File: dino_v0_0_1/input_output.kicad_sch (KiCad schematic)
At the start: 25 parts, among them SW1 SW_DIP_x07

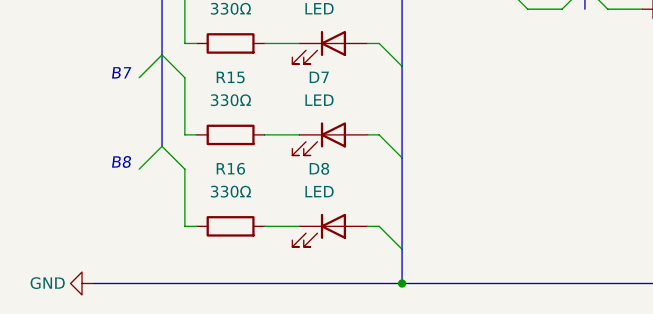
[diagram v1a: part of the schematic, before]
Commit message: Updates schematic with corrections
- Corrects ~CE on 74LS645
- Fixes MCM60256AP DQ6 Pin Number
- Removes "Net Label" for +5V and adds correct text label
- Attaches both GND and VCC to bus proper
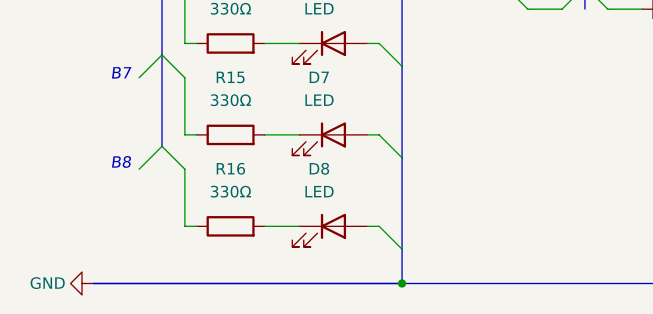
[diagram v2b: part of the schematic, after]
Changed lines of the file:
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@@
 	(title_block
 		(title "Dino v0.0.1")
-		(date "2025-06-15")
-		(rev "v1.0.1")
+		(date "2025-06-30")
+		(rev "v1.0.2")
 		(comment 1 "Input Output Components")
 		(comment 3 "Utilizes a 555 timer and binary counter to increment addressing.")
@@
 		)
 		(stroke
+			(width 0)
+			(type default)
+			(color 0 0 0 1)
+		)
+	)
+	(bus
+		(pts
+			(xy 24.13 119.38) (xy 58.42 119.38)
+		)
+		(stroke

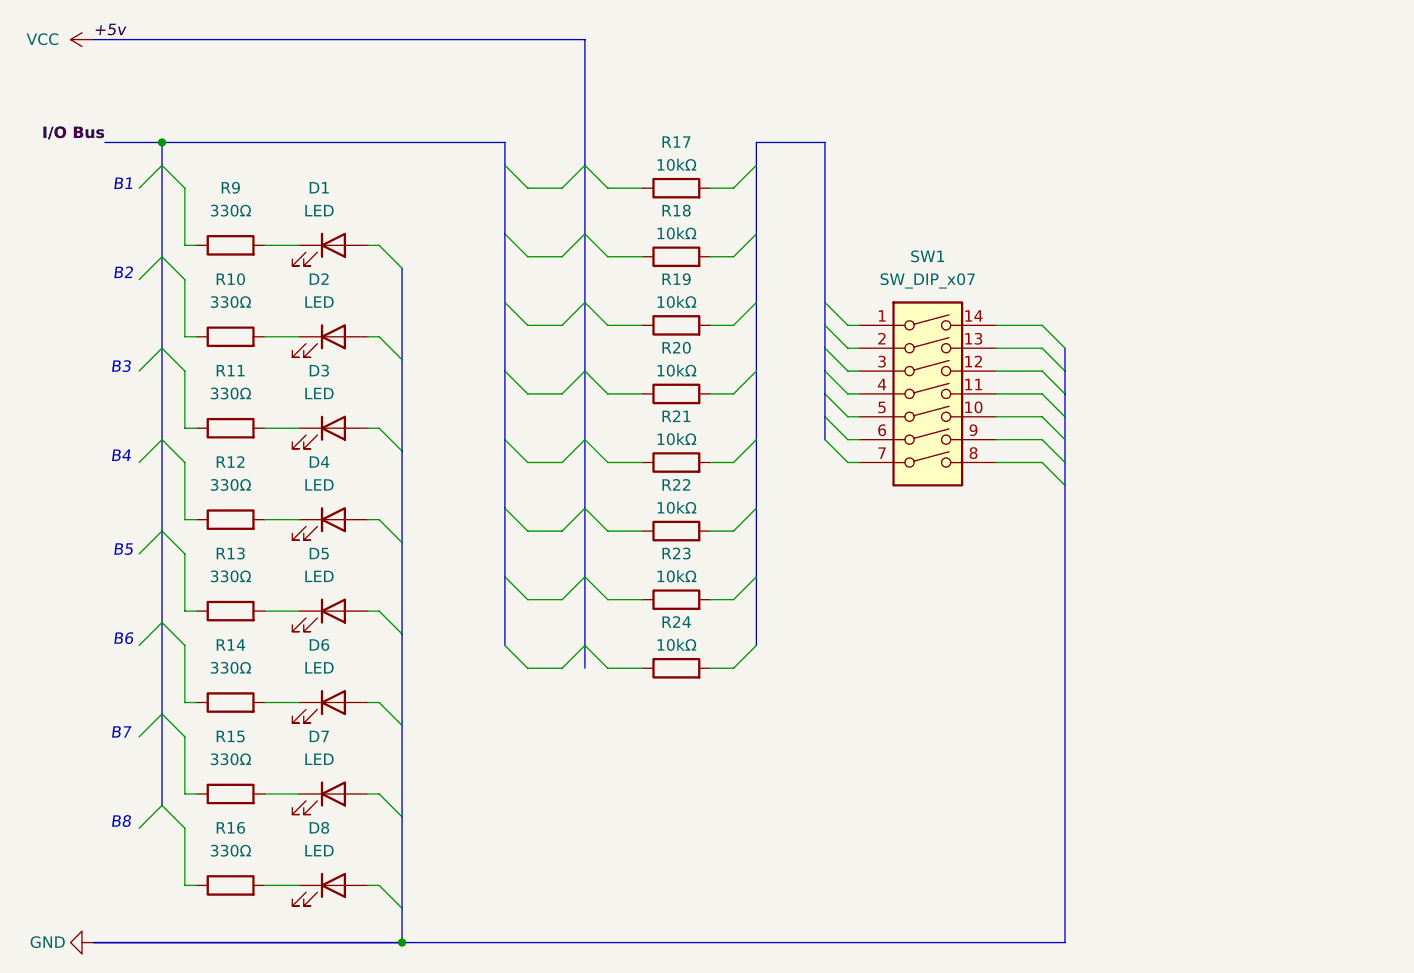
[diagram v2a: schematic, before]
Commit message: Updates schematic for DIP switch change
Replaces 7x DIP switch with 8x DIP switch in schematic.
Modifies connection points and properties accordingly.
Adjusts bus and wire entries for compatibility.
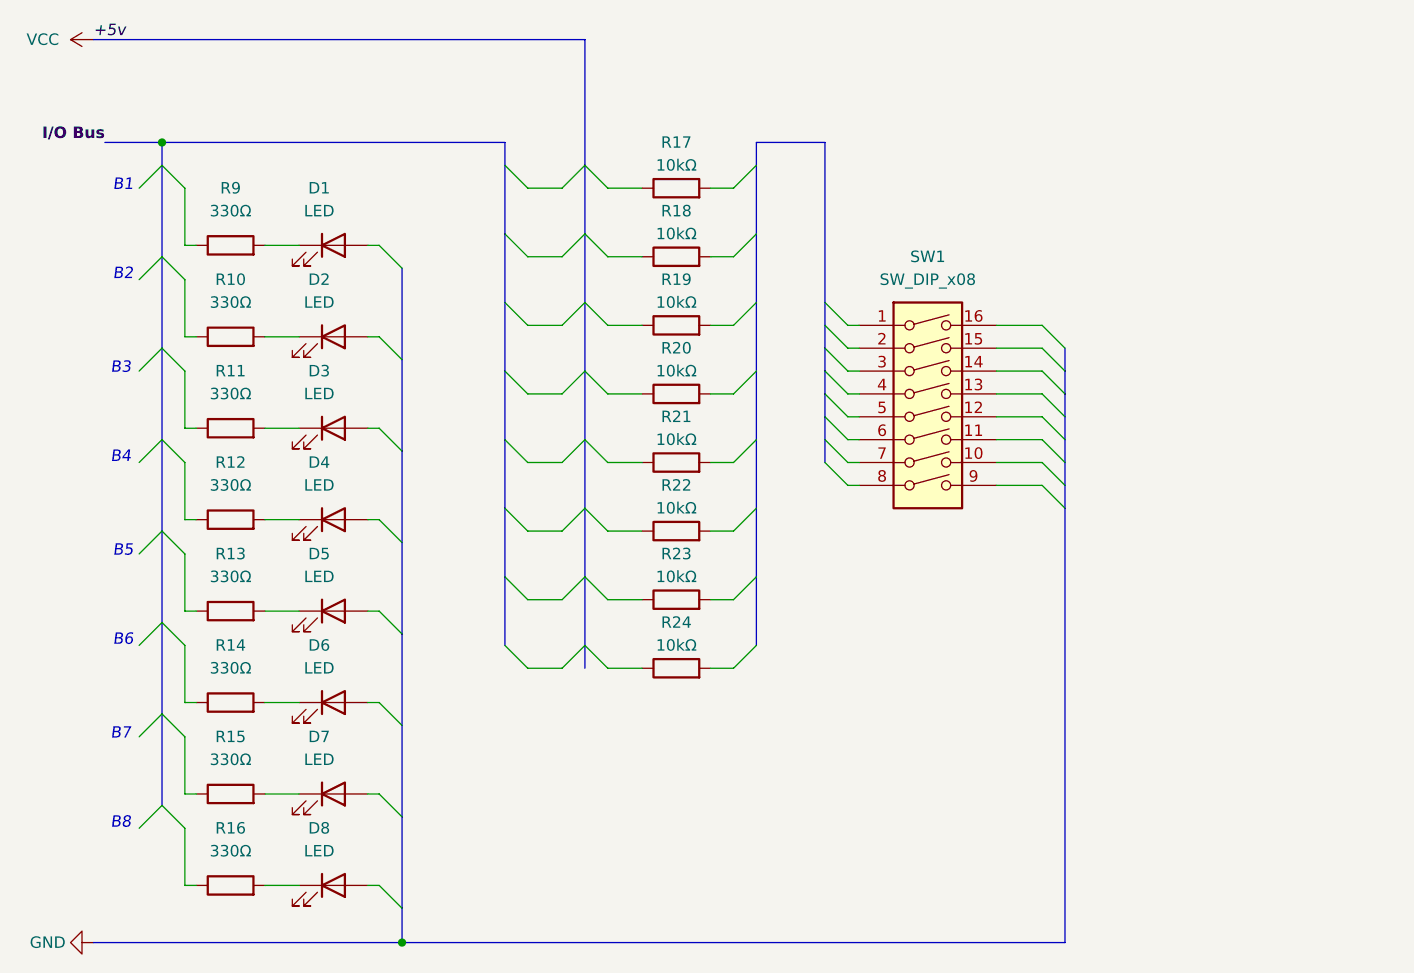
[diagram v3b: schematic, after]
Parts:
- removed SW1: SW_DIP_x07, symbol Switch:SW_DIP_x07
- added SW1: SW_DIP_x08, symbol Switch:SW_DIP_x08
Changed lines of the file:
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@@
 	)
 	(bus_entry
+		(at 105.41 66.04)
+		(size 2.54 2.54)
+		(stroke
+			(width 0)
+			(type default)
+		)
+	)
+	(bus_entry
 		(at 72.39 88.9)
 		(size -2.54 -2.54)
@@
 	)
 	(bus_entry
+		(at 129.54 68.58)
+		(size 2.54 2.54)
+		(stroke
+			(width 0)
+			(type default)
+		)
+	)
+	(bus_entry
 		(at 29.21 86.36)
 		(size 2.54 -2.54)
@@
 		)
 	)
-	(bus
-		(pts
-			(xy 24.13 119.38) (xy 58.42 119.38)
-		)
-		(stroke
-			(width 0)
-			(type default)
-			(color 0 0 0 1)
-		)
-	)
 	(wire
 		(pts
@@
 	(bus
 		(pts
-			(xy 132.08 68.58) (xy 132.08 119.38)
+			(xy 132.08 68.58) (xy 132.08 71.12)
 		)
 		(stroke
@@
 		)
 	)
+	(wire
+		(pts
+			(xy 124.46 68.58) (xy 129.54 68.58)
+		)
+		(stroke
+			(width 0)
+			(type default)
+		)
+	)
 	(bus
 		(pts
@@
 	(bus
 		(pts
+			(xy 132.08 71.12) (xy 132.08 119.38)
+		)
+		(stroke
+			(width 0)
+			(type default)
+			(color 0 0 0 1)
+		)
+	)
+	(bus
+		(pts
 			(xy 78.74 78.74) (xy 78.74 86.36)
 		)
@@
 	(bus
 		(pts
+			(xy 105.41 63.5) (xy 105.41 66.04)
+		)
+		(stroke
+			(width 0)
+			(type default)
+		)
+	)
+	(bus
+		(pts
 			(xy 25.4 30.48) (xy 31.75 30.48)
 		)
@@
 		)
 	)
+	(wire
+		(pts
+			(xy 107.95 68.58) (xy 109.22 68.58)
+		)
+		(stroke
+			(width 0)
+			(type default)
+		)
+	)
 	(bus
 		(pts
@@
 	)
 	(symbol
-		(lib_id "Switch:SW_DIP_x07")
-		(at 116.84 58.42 0)
-		(unit 1)
-		(exclude_from_sim no)
-		(in_bom yes)
-		(on_board yes)
-		(dnp no)
-		(property "Reference" "SW1"
-			(at 116.84 43.18 0)
-			(effects
-				(font
-					(size 1.27 1.27)
-				)
-			)
-		)
-		(property "Value" "SW_DIP_x07"
-			(at 116.84 45.72 0)
-			(effects
-				(font
-					(size 1.27 1.27)
-				)
-			)
-		)
-		(property "Footprint" ""
-			(at 116.84 60.96 0)
-			(effects
-				(font
-					(size 1.27 1.27)
-				)
-				(hide yes)
-			)
-		)
-		(property "Datasheet" "~"
-			(at 116.84 60.96 0)
-			(effects
-				(font
-					(size 1.27 1.27)
-				)
-				(hide yes)
-			)
-		)
-		(property "Description" "7x DIP Switch, Single Pole Single Throw (SPST) switch, small symbol"
-			(at 116.84 58.42 0)
-			(effects
-				(font
-					(size 1.27 1.27)
-				)
-				(hide yes)
-			)
-		)
-		(pin "1"
-		)
-		(pin "3"
-		)
-		(pin "4"
-		)
-		(pin "5"
-		)
-		(pin "6"
-		)
-		(pin "7"
-		)
-		(pin "14"
-		)
-		(pin "13"
-		)
-		(pin "12"
-		)
-		(pin "11"
-		)
-		(pin "10"
-		)
-		(pin "9"
-		)
-		(pin "8"
-		)
-		(pin "2"
-		)
-		(instances
-			(project "dino_v0_0_1"
-				(path "/e43166a5-d972-471d-b3cf-9f4f12c7f541/746aad78-e591-4d08-b628-4d67d677e6d4"
-					(reference "SW1")
-					(unit 1)
-				)
-			)
-		)
-	)
-	(symbol
 		(lib_id "Device:R")
 		(at 39.37 82.55 90)
@@
 					(unit 1)
 				)
+			)
+		)
+	)
+	(symbol
+		(lib_id "Switch:SW_DIP_x08")
+		(at 116.84 60.96 0)
+		(unit 1)
+		(exclude_from_sim no)
+		(in_bom yes)
+		(on_board yes)
+		(dnp no)
+		(fields_autoplaced yes)
+		(property "Reference" "SW1"
+			(at 116.84 43.18 0)
+			(effects
+				(font
+					(size 1.27 1.27)
+				)
+			)
+		)
+		(property "Value" "SW_DIP_x08"
+			(at 116.84 45.72 0)
+			(effects
+				(font
+					(size 1.27 1.27)
+				)
+			)
+		)
+		(property "Footprint" ""
+			(at 116.84 60.96 0)
+			(effects
+				(font
+					(size 1.27 1.27)
+				)
+				(hide yes)
+			)
+		)
+		(property "Datasheet" "~"
+			(at 116.84 60.96 0)
+			(effects
+				(font
+					(size 1.27 1.27)
+				)
+				(hide yes)
+			)
+		)
+		(property "Description" "8x DIP Switch, Single Pole Single Throw (SPST) switch, small symbol"
+			(at 116.84 60.96 0)
+			(effects
+				(font
+					(size 1.27 1.27)
+				)
+				(hide yes)
+			)
+		)
+		(pin "14"
+		)
+		(pin "13"
+		)
+		(pin "12"
+		)
+		(pin "11"
+		)
+		(pin "10"
+		)
+		(pin "9"
+		)
+		(pin "2"
+		)
+		(pin "3"
+		)
+		(pin "4"
+		)
+		(pin "5"
+		)
+		(pin "6"
+		)
+		(pin "7"
+		)
+		(pin "8"
+		)
+		(pin "16"
+		)
+		(pin "15"
+		)
+		(pin "1"
+		)
+		(instances
+			(project ""
+				(path "/e43166a5-d972-471d-b3cf-9f4f12c7f541/746aad78-e591-4d08-b628-4d67d677e6d4"
+					(reference "SW1")
+					(unit 1)
+				)

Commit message: Refactors circuit schematic and adds component
Repositions resistors and re-routes junctions for optimized layout.
Introduces 74LS244N component to enhance functionality.
Updates buses and wires for improved organization and signal integrity.
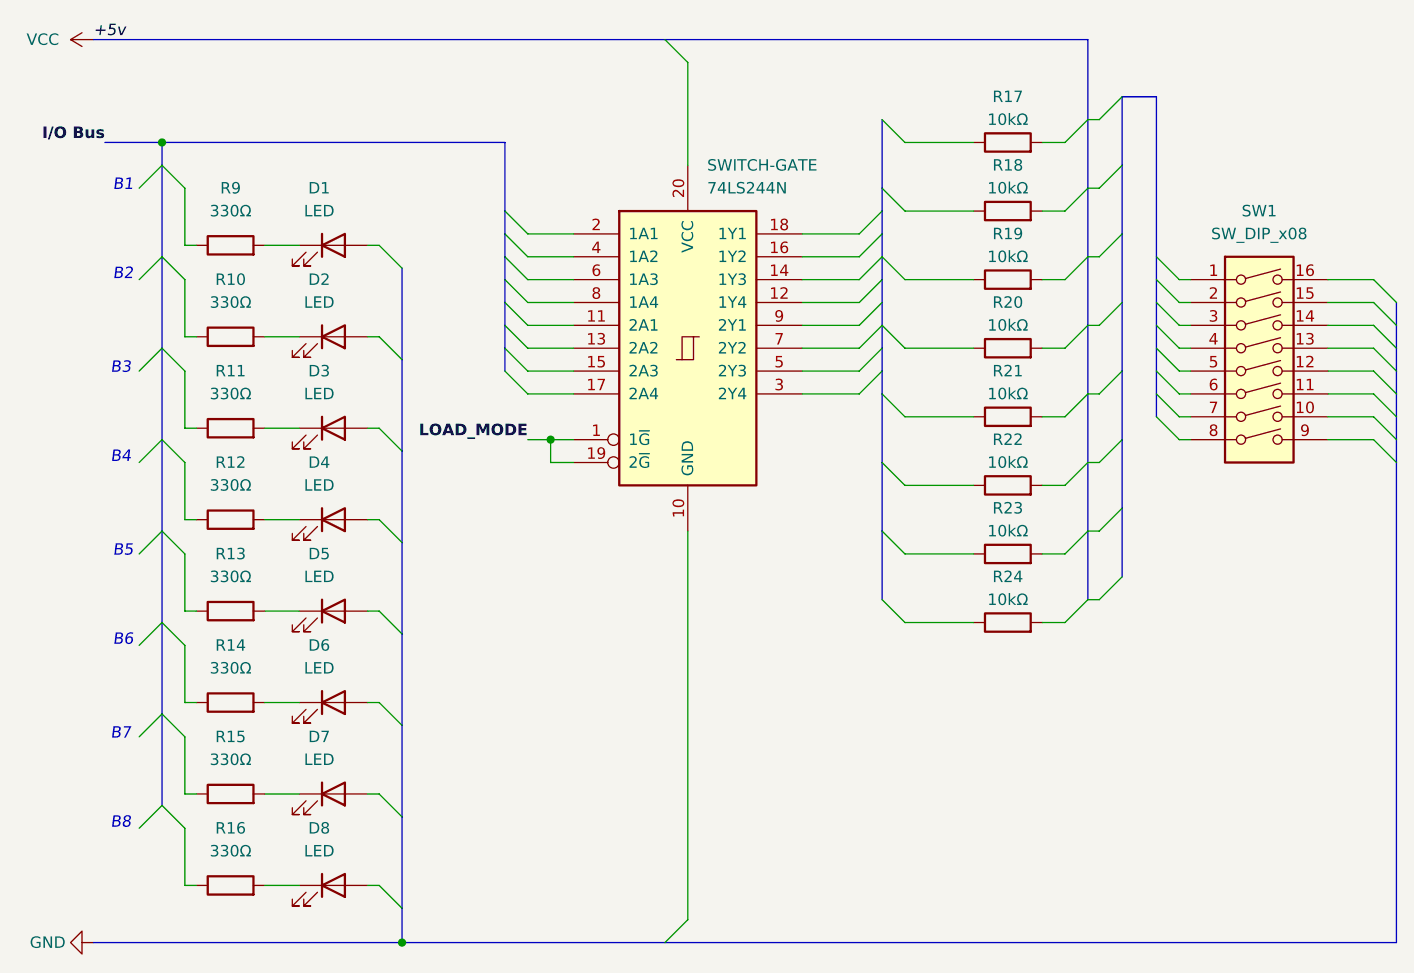
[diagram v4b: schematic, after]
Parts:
- added SWITCH-GATE: 74LS244N, symbol 74xx:74LS244N
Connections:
- new net LOAD_MODE: SWITCH-GATE.1 (1~{G}), SWITCH-GATE.19 (2~{G})
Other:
- moved on the sheet: R17, R18, R19, R20, R21, R22, R23, R24, SW1
